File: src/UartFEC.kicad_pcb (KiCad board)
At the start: 2 copper layers, 24 x 27.9 mm, 16 parts, among them J1 B3B-XH-A, P1 105444-0001, U1 FT232RL

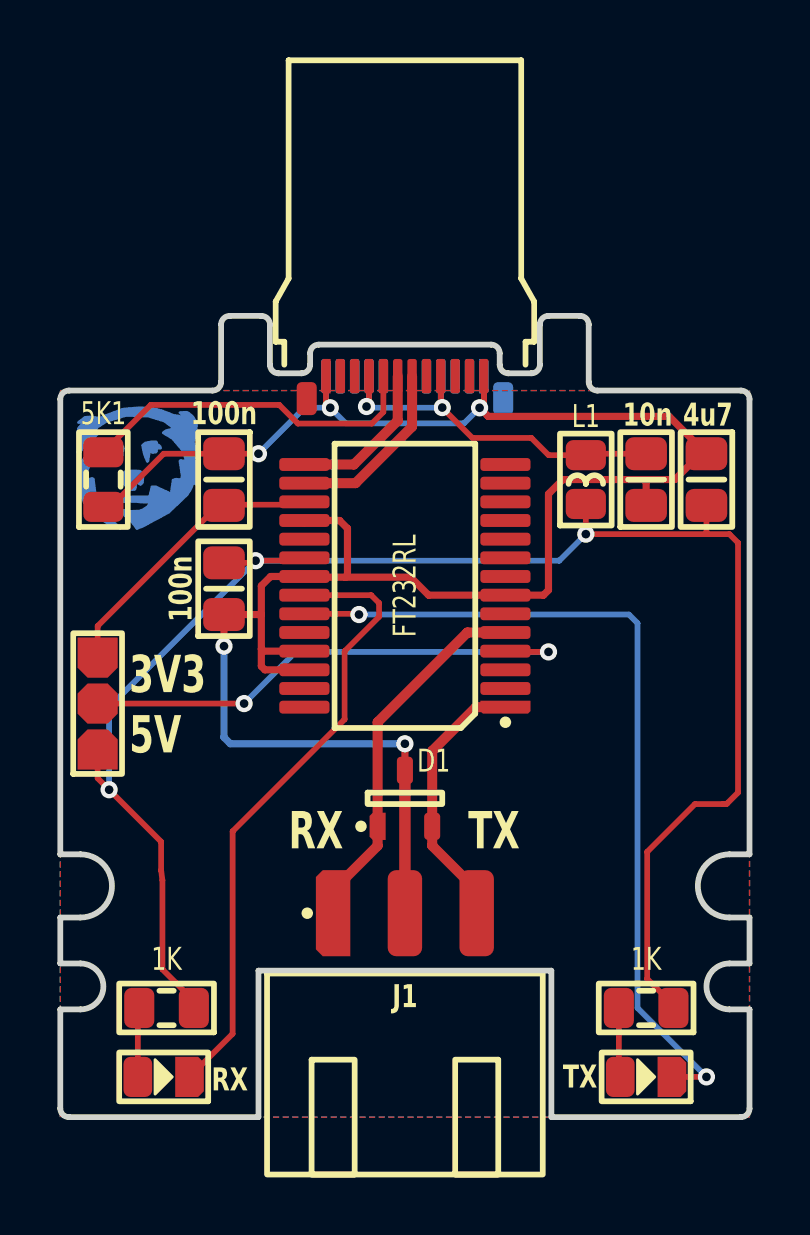
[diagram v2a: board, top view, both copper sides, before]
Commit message: Swapping L1 and 10nF location
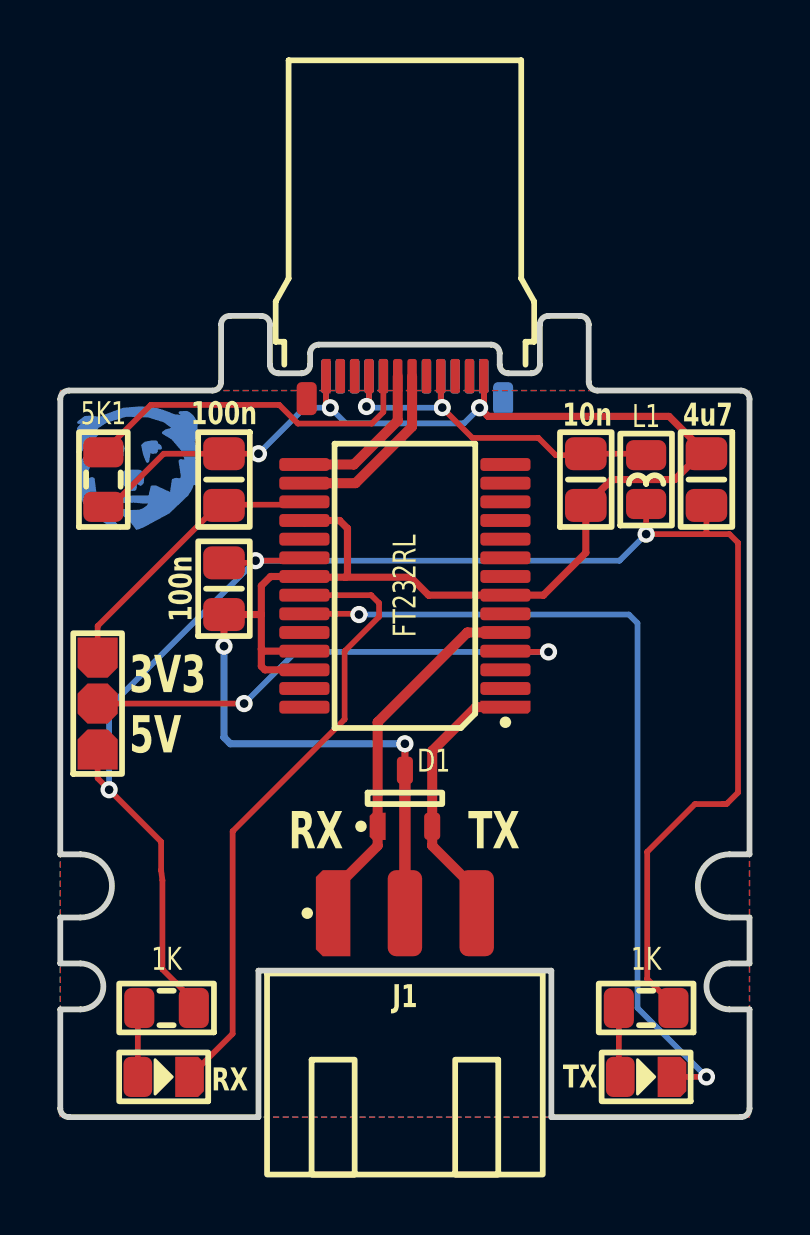
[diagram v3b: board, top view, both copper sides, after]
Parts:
- moved C1 2.10 mm to (38.3, 25.7)
- moved L1 2.10 mm to (40.4, 25.7)
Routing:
- net GND: track 76.9 -> 75.0 mm
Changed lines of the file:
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@@
   )
   (footprint "Medo64:L (0805)" (layer "F.Cu")
-    (at 38.3 25.7 90)
+    (at 40.4 25.7 90)
     (descr "RESC2013X70N")
     (attr smd)
@@
   )
   (footprint "Medo64:C (0805)" (layer "F.Cu")
-    (at 40.4 25.7 90)
+    (at 38.3 25.7 90)
     (tags "CAPC2013X140N")
     (attr smd)
@@
   (segment (start 32.95 35.15) (end 34.475 33.625) (width 0.35) (layer "F.Cu") (net 2))
   (segment (start 23.556148 39.656148) (end 23.556148 42.756148) (width 0.2) (layer "F.Cu") (net 3))
-  (segment (start 38.3 27.6) (end 38.3 26.55) (width 0.2) (layer "F.Cu") (net 3))
   (segment (start 43.211786 36.988214) (end 43.208226 36.9881) (width 0.2) (layer "F.Cu") (net 3))
   (segment (start 43.3 27.6) (end 43.6 27.9) (width 0.2) (layer "F.Cu") (net 3))
@@
   (segment (start 42.5 26.6) (end 42.5 27.6) (width 0.2) (layer "F.Cu") (net 3))
   (segment (start 28.5 28.525) (end 26.8 28.525) (width 0.2) (layer "F.Cu") (net 3))
-  (segment (start 42.5 27.6) (end 38.3 27.6) (width 0.2) (layer "F.Cu") (net 3))
   (segment (start 21.7 36.5) (end 23.510568 38.310568) (width 0.2) (layer "F.Cu") (net 3))
+  (segment (start 40.400008 27.6) (end 42.5 27.6) (width 0.2) (layer "F.Cu") (net 3))
   (segment (start 43.6 36.6) (end 43.211786 36.988214) (width 0.2) (layer "F.Cu") (net 3))
   (segment (start 26.725 28.6) (end 26.8 28.525) (width 0.2) (layer "F.Cu") (net 3))
   (segment (start 43.208226 36.9881) (end 43.08487 37) (width 0.2) (layer "F.Cu") (net 3))
+  (segment (start 40.4 27.599992) (end 40.400008 27.6) (width 0.2) (layer "F.Cu") (net 3))
+  (segment (start 40.4 26.55) (end 40.4 27.599992) (width 0.2) (layer "F.Cu") (net 3))
   (segment (start 21.7 36.5) (end 21.3 36.1) (width 0.2) (layer "F.Cu") (net 3))
   (segment (start 40.436628 43.086628) (end 41.4 44.05) (width 0.2) (layer "F.Cu") (net 3))
@@
   (segment (start 43.08487 37) (end 42.101103 37) (width 0.2) (layer "F.Cu") (net 3))
   (via (at 26.8 28.525) (size 0.6) (drill 0.3) (layers "F.Cu" "B.Cu") (net 3))
-  (via (at 38.3 27.6) (size 0.6) (drill 0.3) (layers "F.Cu" "B.Cu") (net 3))
+  (via (at 40.400008 27.6) (size 0.6) (drill 0.3) (layers "F.Cu" "B.Cu") (net 3))
   (via (at 21.7 36.5) (size 0.6) (drill 0.3) (layers "F.Cu" "B.Cu") (net 3))
   (segment (start 26.8 28.525) (end 21.7 33.625) (width 0.2) (layer "B.Cu") (net 3))
-  (segment (start 37.375 28.525) (end 38.3 27.6) (width 0.2) (layer "B.Cu") (net 3))
+  (segment (start 39.475008 28.525) (end 40.400008 27.6) (width 0.2) (layer "B.Cu") (net 3))
   (segment (start 21.7 33.625) (end 21.7 36.5) (width 0.2) (layer "B.Cu") (net 3))
-  (segment (start 26.8 28.525) (end 37.375 28.525) (width 0.2) (layer "B.Cu") (net 3))
+  (segment (start 26.8 28.525) (end 39.475008 28.525) (width 0.2) (layer "B.Cu") (net 3))
   (segment (start 29.5 40) (end 31.05 38.45) (width 0.35) (layer "F.Cu") (net 4))
   (segment (start 31.05 34.15) (end 34.175 31.025) (width 0.35) (layer "F.Cu") (net 4))
@@
   (segment (start 34.75 22.1) (end 34.75 23.05) (width 0.2) (layer "F.Cu") (net 7))
   (segment (start 27.075 31.675) (end 27 31.6) (width 0.25) (layer "F.Cu") (net 7))
-  (segment (start 41.4 25.7) (end 42.3 24.8) (width 0.25) (layer "F.Cu") (net 7))
+  (segment (start 38.3 28.25) (end 36.825 29.725) (width 0.25) (layer "F.Cu") (net 7))
+  (segment (start 28.525 29.1) (end 29.925 29.1) (width 0.25) (layer "F.Cu") (net 7))
   (segment (start 36.825 29.725) (end 32.825 29.725) (width 0.25) (layer "F.Cu") (net 7))
-  (segment (start 28.525 29.1) (end 29.925 29.1) (width 0.25) (layer "F.Cu") (net 7))
+  (segment (start 38.3 26.6) (end 38.3 28.25) (width 0.25) (layer "F.Cu") (net 7))
   (segment (start 25.7 30.4) (end 27 30.4) (width 0.25) (layer "F.Cu") (net 7))
   (segment (start 26.9 24.8) (end 25.7 24.8) (width 0.2) (layer "F.Cu") (net 7))
-  (segment (start 37 29.55) (end 36.825 29.725) (width 0.25) (layer "F.Cu") (net 7))
+  (segment (start 39.2 25.7) (end 38.3 26.6) (width 0.25) (layer "F.Cu") (net 7))
   (segment (start 30 27.4) (end 30 29.025) (width 0.25) (layer "F.Cu") (net 7))
   (segment (start 32 40.8) (end 32 35.825) (width 0.4) (layer "F.Cu") (net 7))
-  (segment (start 40.325 25.7) (end 41.4 25.7) (width 0.25) (layer "F.Cu") (net 7))
   (segment (start 34.9 23.5) (end 41.2 23.5) (width 0.25) (layer "F.Cu") (net 7))
   (segment (start 25.7 31.5) (end 25.7 30.4) (width 0.25) (layer "F.Cu") (net 7))
   (segment (start 34.75 22.95697) (end 34.75 22.1) (width 0.2) (layer "F.Cu") (net 7))
   (segment (start 27 32.2) (end 27 31.6) (width 0.25) (layer "F.Cu") (net 7))
-  (segment (start 40.4 26.6) (end 40.4 25.775) (width 0.25) (layer "F.Cu") (net 7))
   (segment (start 28.5 31.675) (end 27.075 31.675) (width 0.25) (layer "F.Cu") (net 7))
   (segment (start 41.2 23.5) (end 42.5 24.8) (width 0.25) (layer "F.Cu") (net 7))
   (segment (start 28.5 27.225) (end 28.6 27.125) (width 0.25) (layer "F.Cu") (net 7))
+  (segment (start 42.3 24.8) (end 41.4 25.7) (width 0.25) (layer "F.Cu") (net 7))
   (segment (start 32.825 29.725) (end 32.2 29.1) (width 0.25) (layer "F.Cu") (net 7))
-  (segment (start 40.325 25.7) (end 40.4 25.775) (width 0.25) (layer "F.Cu") (net 7))
   (segment (start 27.325 29.075) (end 28.5 29.075) (width 0.25) (layer "F.Cu") (net 7))
   (segment (start 27 30.4) (end 27 29.4) (width 0.25) (layer "F.Cu") (net 7))
   (segment (start 29.25 23.05) (end 29.4 23.2) (width 0.2) (layer "F.Cu") (net 7))
-  (segment (start 40.325 25.7) (end 37.5 25.7) (width 0.25) (layer "F.Cu") (net 7))
   (segment (start 30 29.025) (end 29.925 29.1) (width 0.25) (layer "F.Cu") (net 7))
-  (segment (start 37 26.2) (end 37 29.55) (width 0.25) (layer "F.Cu") (net 7))
   (segment (start 29.725 27.125) (end 30 27.4) (width 0.25) (layer "F.Cu") (net 7))
   (segment (start 34.75 23.05) (end 34.6 23.2) (width 0.2) (layer "F.Cu") (net 7))
@@
   (segment (start 34.50697 23.2) (end 34.75 22.95697) (width 0.2) (layer "F.Cu") (net 7))
   (segment (start 27 30.4) (end 27 31.6) (width 0.25) (layer "F.Cu") (net 7))
-  (segment (start 37.5 25.7) (end 37 26.2) (width 0.25) (layer "F.Cu") (net 7))
+  (segment (start 32.2 29.1) (end 29.925 29.1) (width 0.25) (layer "F.Cu") (net 7))
   (segment (start 28.6 27.125) (end 29.725 27.125) (width 0.25) (layer "F.Cu") (net 7))
   (segment (start 21.75 26.65) (end 23.6 24.8) (width 0.2) (layer "F.Cu") (net 7))
+  (segment (start 41.4 25.7) (end 39.2 25.7) (width 0.25) (layer "F.Cu") (net 7))
   (segment (start 32 35.825) (end 32 34.9) (width 0.25) (layer "F.Cu") (net 7))
   (segment (start 28.5 32.325) (end 27.125 32.325) (width 0.25) (layer "F.Cu") (net 7))
-  (segment (start 32.2 29.1) (end 29.925 29.1) (width 0.25) (layer "F.Cu") (net 7))
   (via (at 25.7 31.5) (size 0.6) (drill 0.3) (layers "F.Cu" "B.Cu") (net 7))
   (via (at 32 34.9) (size 0.6) (drill 0.3) (layers "F.Cu" "B.Cu") (net 7))
@@
   (segment (start 29.4 23.2) (end 28.5 23.2) (width 0.2) (layer "B.Cu") (net 7))
   (segment (start 30.75 22.1) (end 30.75 23.070102) (width 0.2) (layer "F.Cu") (net 8))
-  (segment (start 36.405026 24.25) (end 37.005026 24.85) (width 0.2) (layer "F.Cu") (net 8))
-  (segment (start 37.005026 24.85) (end 38.3 24.85) (width 0.2) (layer "F.Cu") (net 8))
+  (segment (start 33.25 22.1) (end 33.25 23.15) (width 0.2) (layer "F.Cu") (net 8))
+  (segment (start 37.25 24.85) (end 38.3 24.85) (width 0.2) (layer "F.Cu") (net 8))
   (segment (start 30.75 23.070102) (end 30.663983 23.156119) (width 0.2) (layer "F.Cu") (net 8))
-  (segment (start 34.35 24.25) (end 36.405026 24.25) (width 0.2) (layer "F.Cu") (net 8))
+  (segment (start 34.35 24.25) (end 36.65 24.25) (width 0.2) (layer "F.Cu") (net 8))
   (segment (start 40.4 24.8) (end 38.35 24.8) (width 0.2) (layer "F.Cu") (net 8))
-  (segment (start 33.25 22.1) (end 33.25 23.15) (width 0.2) (layer "F.Cu") (net 8))
   (segment (start 33.25 23.15) (end 34.35 24.25) (width 0.2) (layer "F.Cu") (net 8))
+  (segment (start 36.65 24.25) (end 37.25 24.85) (width 0.2) (layer "F.Cu") (net 8))
   (via (at 30.663983 23.156119) (size 0.6) (drill 0.3) (layers "F.Cu" "B.Cu") (net 8))
   (via (at 33.3 23.192136) (size 0.6) (drill 0.3) (layers "F.Cu" "B.Cu") (net 8))

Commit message: Added RTS/CTS loopback
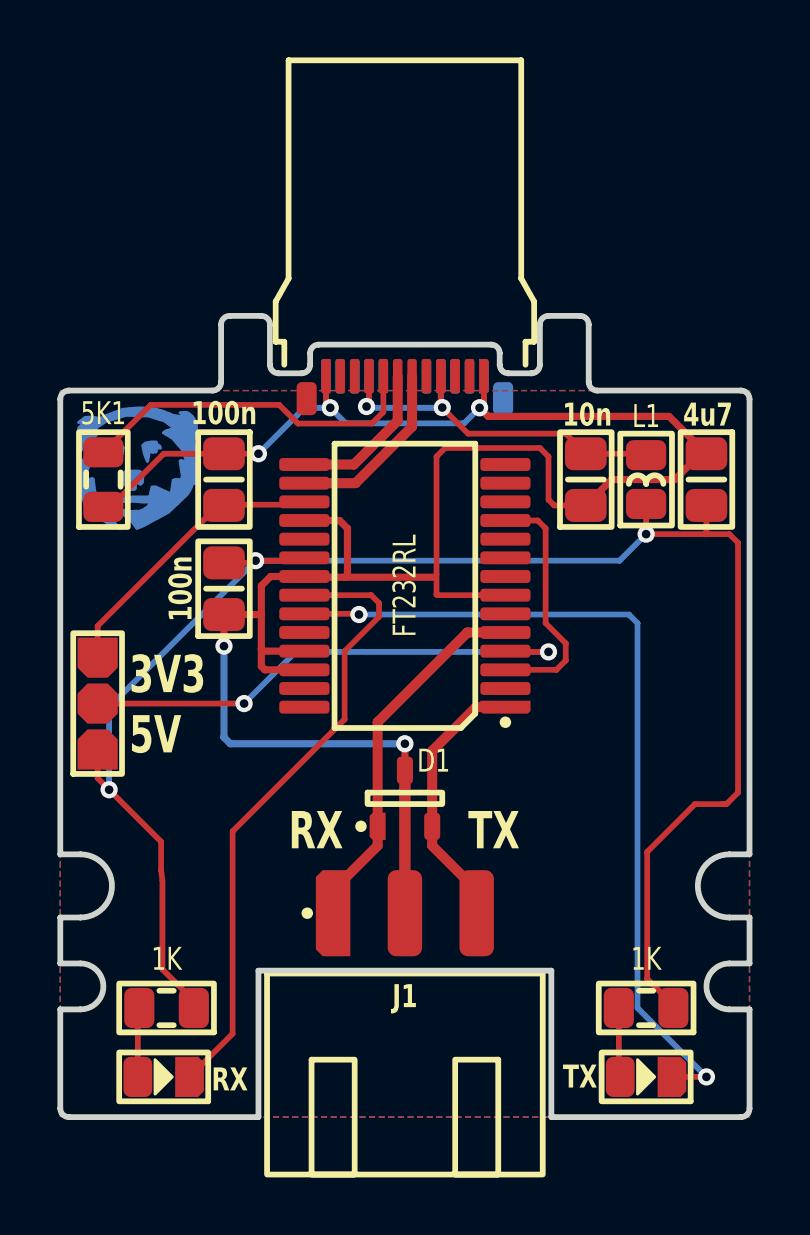
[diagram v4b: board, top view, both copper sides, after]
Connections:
- U1 pad 11: (no net) -> RTS_CTS
- U1 pad 3: (no net) -> RTS_CTS
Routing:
- net RTS_CTS: track 0.00 -> 8.64 mm
- net GND: track 75.0 -> 81.2 mm
- net TXD: track 9.47 -> 8.67 mm
- net RXD: track 13.0 -> 12.2 mm
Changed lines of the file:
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@@
   (net 13 "LED_RXD'")
   (net 14 "LED_RXD")
+  (net 15 "RTS_CTS")
   (footprint "Medo64:R (0805)" (layer "F.Cu")
     (at 40.4 44.1 180)
@@
       (thermal_bridge_angle 45))
     (pad "3" smd roundrect locked (at -3.5 -2.925 180) (size 1.75 0.45) (layers "F.Cu" "F.Paste" "F.Mask") (roundrect_rratio 0.25)
-      (thermal_bridge_angle 45))
+      (net 15 "RTS_CTS") (thermal_bridge_angle 45))
     (pad "4" smd roundrect locked (at -3.5 -2.275 180) (size 1.75 0.45) (layers "F.Cu" "F.Paste" "F.Mask") (roundrect_rratio 0.25)
       (net 10 "Vio") (thermal_bridge_angle 45))
@@
       (thermal_bridge_angle 45))
     (pad "11" smd roundrect locked (at -3.5 2.275 180) (size 1.75 0.45) (layers "F.Cu" "F.Paste" "F.Mask") (roundrect_rratio 0.25)
-      (thermal_bridge_angle 45))
+      (net 15 "RTS_CTS") (thermal_bridge_angle 45))
     (pad "12" smd roundrect locked (at -3.5 2.925 180) (size 1.75 0.45) (layers "F.Cu" "F.Paste" "F.Mask") (roundrect_rratio 0.25)
       (thermal_bridge_angle 45))
@@
   (segment (start 34.5 40) (end 32.95 38.45) (width 0.35) (layer "F.Cu") (net 2))
   (segment (start 34.475 33.625) (end 35.5 33.625) (width 0.35) (layer "F.Cu") (net 2))
-  (segment (start 34.5 40.8) (end 34.5 40) (width 0.35) (layer "F.Cu") (net 2))
   (segment (start 32.95 35.15) (end 34.475 33.625) (width 0.35) (layer "F.Cu") (net 2))
   (segment (start 23.556148 39.656148) (end 23.556148 42.756148) (width 0.2) (layer "F.Cu") (net 3))
@@
   (segment (start 31.05 34.15) (end 34.175 31.025) (width 0.35) (layer "F.Cu") (net 4))
   (segment (start 31.05 37.775) (end 31.05 34.15) (width 0.35) (layer "F.Cu") (net 4))
-  (segment (start 29.5 40.8) (end 29.5 40) (width 0.35) (layer "F.Cu") (net 4))
   (segment (start 34.175 31.025) (end 35.5 31.025) (width 0.35) (layer "F.Cu") (net 4))
   (segment (start 31.05 38.45) (end 31.05 37.775) (width 0.35) (layer "F.Cu") (net 4))
@@
   (segment (start 32.25 22.1) (end 32.25 23.856587) (width 0.35) (layer "F.Cu") (net 6))
   (segment (start 32.25 23.856587) (end 30.281587 25.825) (width 0.35) (layer "F.Cu") (net 6))
+  (segment (start 33.1 24.9) (end 33.4 24.6) (width 0.2) (layer "F.Cu") (net 7))
   (segment (start 27.125 32.325) (end 27 32.2) (width 0.25) (layer "F.Cu") (net 7))
+  (segment (start 33.1 29) (end 33.1 24.9) (width 0.2) (layer "F.Cu") (net 7))
+  (segment (start 37 24.9) (end 37 26.4) (width 0.2) (layer "F.Cu") (net 7))
   (segment (start 27 29.4) (end 27.325 29.075) (width 0.25) (layer "F.Cu") (net 7))
   (segment (start 34.75 22.1) (end 34.75 23.05) (width 0.2) (layer "F.Cu") (net 7))
   (segment (start 27.075 31.675) (end 27 31.6) (width 0.25) (layer "F.Cu") (net 7))
-  (segment (start 38.3 28.25) (end 36.825 29.725) (width 0.25) (layer "F.Cu") (net 7))
+  (segment (start 33.1 29.7) (end 33.1 29) (width 0.2) (layer "F.Cu") (net 7))
   (segment (start 28.525 29.1) (end 29.925 29.1) (width 0.25) (layer "F.Cu") (net 7))
-  (segment (start 36.825 29.725) (end 32.825 29.725) (width 0.25) (layer "F.Cu") (net 7))
-  (segment (start 38.3 26.6) (end 38.3 28.25) (width 0.25) (layer "F.Cu") (net 7))
   (segment (start 25.7 30.4) (end 27 30.4) (width 0.25) (layer "F.Cu") (net 7))
   (segment (start 26.9 24.8) (end 25.7 24.8) (width 0.2) (layer "F.Cu") (net 7))
+  (segment (start 33.125 29.725) (end 33.1 29.7) (width 0.2) (layer "F.Cu") (net 7))
   (segment (start 39.2 25.7) (end 38.3 26.6) (width 0.25) (layer "F.Cu") (net 7))
   (segment (start 30 27.4) (end 30 29.025) (width 0.25) (layer "F.Cu") (net 7))
@@
   (segment (start 34.9 23.5) (end 41.2 23.5) (width 0.25) (layer "F.Cu") (net 7))
   (segment (start 25.7 31.5) (end 25.7 30.4) (width 0.25) (layer "F.Cu") (net 7))
+  (segment (start 29.925 29.1) (end 33 29.1) (width 0.25) (layer "F.Cu") (net 7))
   (segment (start 34.75 22.95697) (end 34.75 22.1) (width 0.2) (layer "F.Cu") (net 7))
   (segment (start 27 32.2) (end 27 31.6) (width 0.25) (layer "F.Cu") (net 7))
+  (segment (start 36.7 24.6) (end 37 24.9) (width 0.2) (layer "F.Cu") (net 7))
   (segment (start 28.5 31.675) (end 27.075 31.675) (width 0.25) (layer "F.Cu") (net 7))
   (segment (start 41.2 23.5) (end 42.5 24.8) (width 0.25) (layer "F.Cu") (net 7))
-  (segment (start 28.5 27.225) (end 28.6 27.125) (width 0.25) (layer "F.Cu") (net 7))
   (segment (start 42.3 24.8) (end 41.4 25.7) (width 0.25) (layer "F.Cu") (net 7))
-  (segment (start 32.825 29.725) (end 32.2 29.1) (width 0.25) (layer "F.Cu") (net 7))
   (segment (start 27.325 29.075) (end 28.5 29.075) (width 0.25) (layer "F.Cu") (net 7))
   (segment (start 27 30.4) (end 27 29.4) (width 0.25) (layer "F.Cu") (net 7))
+  (segment (start 37.2 26.6) (end 38.3 26.6) (width 0.2) (layer "F.Cu") (net 7))
   (segment (start 29.25 23.05) (end 29.4 23.2) (width 0.2) (layer "F.Cu") (net 7))
+  (segment (start 33.4 24.6) (end 36.7 24.6) (width 0.2) (layer "F.Cu") (net 7))
   (segment (start 30 29.025) (end 29.925 29.1) (width 0.25) (layer "F.Cu") (net 7))
   (segment (start 29.725 27.125) (end 30 27.4) (width 0.25) (layer "F.Cu") (net 7))
@@
   (segment (start 29.25 22.1) (end 29.25 23.05) (width 0.2) (layer "F.Cu") (net 7))
   (segment (start 34.50697 23.2) (end 34.75 22.95697) (width 0.2) (layer "F.Cu") (net 7))
+  (segment (start 37 26.4) (end 37.2 26.6) (width 0.2) (layer "F.Cu") (net 7))
   (segment (start 27 30.4) (end 27 31.6) (width 0.25) (layer "F.Cu") (net 7))
-  (segment (start 32.2 29.1) (end 29.925 29.1) (width 0.25) (layer "F.Cu") (net 7))
   (segment (start 28.6 27.125) (end 29.725 27.125) (width 0.25) (layer "F.Cu") (net 7))
   (segment (start 21.75 26.65) (end 23.6 24.8) (width 0.2) (layer "F.Cu") (net 7))
   (segment (start 41.4 25.7) (end 39.2 25.7) (width 0.25) (layer "F.Cu") (net 7))
   (segment (start 32 35.825) (end 32 34.9) (width 0.25) (layer "F.Cu") (net 7))
+  (segment (start 35.5 29.725) (end 33.125 29.725) (width 0.2) (layer "F.Cu") (net 7))
   (segment (start 28.5 32.325) (end 27.125 32.325) (width 0.25) (layer "F.Cu") (net 7))
   (via (at 25.7 31.5) (size 0.6) (drill 0.3) (layers "F.Cu" "B.Cu") (net 7))
@@
   (segment (start 34.75 23.05) (end 34.6 23.2) (width 0.2) (layer "B.Cu") (net 7))
   (segment (start 29.4 23.2) (end 28.5 23.2) (width 0.2) (layer "B.Cu") (net 7))
+  (segment (start 33.25 23.15) (end 34.2 24.1) (width 0.2) (layer "F.Cu") (net 8))
   (segment (start 30.75 22.1) (end 30.75 23.070102) (width 0.2) (layer "F.Cu") (net 8))
+  (segment (start 30.75 23.070102) (end 30.663983 23.156119) (width 0.2) (layer "F.Cu") (net 8))
   (segment (start 33.25 22.1) (end 33.25 23.15) (width 0.2) (layer "F.Cu") (net 8))
-  (segment (start 37.25 24.85) (end 38.3 24.85) (width 0.2) (layer "F.Cu") (net 8))
-  (segment (start 30.75 23.070102) (end 30.663983 23.156119) (width 0.2) (layer "F.Cu") (net 8))
-  (segment (start 34.35 24.25) (end 36.65 24.25) (width 0.2) (layer "F.Cu") (net 8))
   (segment (start 40.4 24.8) (end 38.35 24.8) (width 0.2) (layer "F.Cu") (net 8))
-  (segment (start 33.25 23.15) (end 34.35 24.25) (width 0.2) (layer "F.Cu") (net 8))
-  (segment (start 36.65 24.25) (end 37.25 24.85) (width 0.2) (layer "F.Cu") (net 8))
+  (segment (start 37.6 24.1) (end 38.3 24.8) (width 0.2) (layer "F.Cu") (net 8))
+  (segment (start 34.2 24.1) (end 37.6 24.1) (width 0.2) (layer "F.Cu") (net 8))
   (via (at 30.663983 23.156119) (size 0.6) (drill 0.3) (layers "F.Cu" "B.Cu") (net 8))
   (via (at 33.3 23.192136) (size 0.6) (drill 0.3) (layers "F.Cu" "B.Cu") (net 8))
@@
   (segment (start 31.1 30) (end 30.825 29.725) (width 0.2) (layer "F.Cu") (net 14))
   (segment (start 29.9 34.05) (end 29.9 31.677814) (width 0.2) (layer "F.Cu") (net 14))
+  (segment (start 35.5 32.325) (end 37.275 32.325) (width 0.2) (layer "F.Cu") (net 15))
+  (segment (start 37.6 31.4) (end 36.9 30.7) (width 0.2) (layer "F.Cu") (net 15))
+  (segment (start 37.6 32) (end 37.6 31.4) (width 0.2) (layer "F.Cu") (net 15))
+  (segment (start 36.9 30.7) (end 36.9 27.4) (width 0.2) (layer "F.Cu") (net 15))
+  (segment (start 36.625 27.125) (end 35.5 27.125) (width 0.2) (layer "F.Cu") (net 15))
+  (segment (start 37.275 32.325) (end 37.6 32) (width 0.2) (layer "F.Cu") (net 15))
+  (segment (start 36.9 27.4) (end 36.625 27.125) (width 0.2) (layer "F.Cu") (net 15))
   (zone (net 7) (net_name "GND") (layers "F&B.Cu") (hatch edge 0.5)
     (connect_pads (clearance 0.25))
